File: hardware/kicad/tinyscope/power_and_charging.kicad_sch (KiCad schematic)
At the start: 44 parts

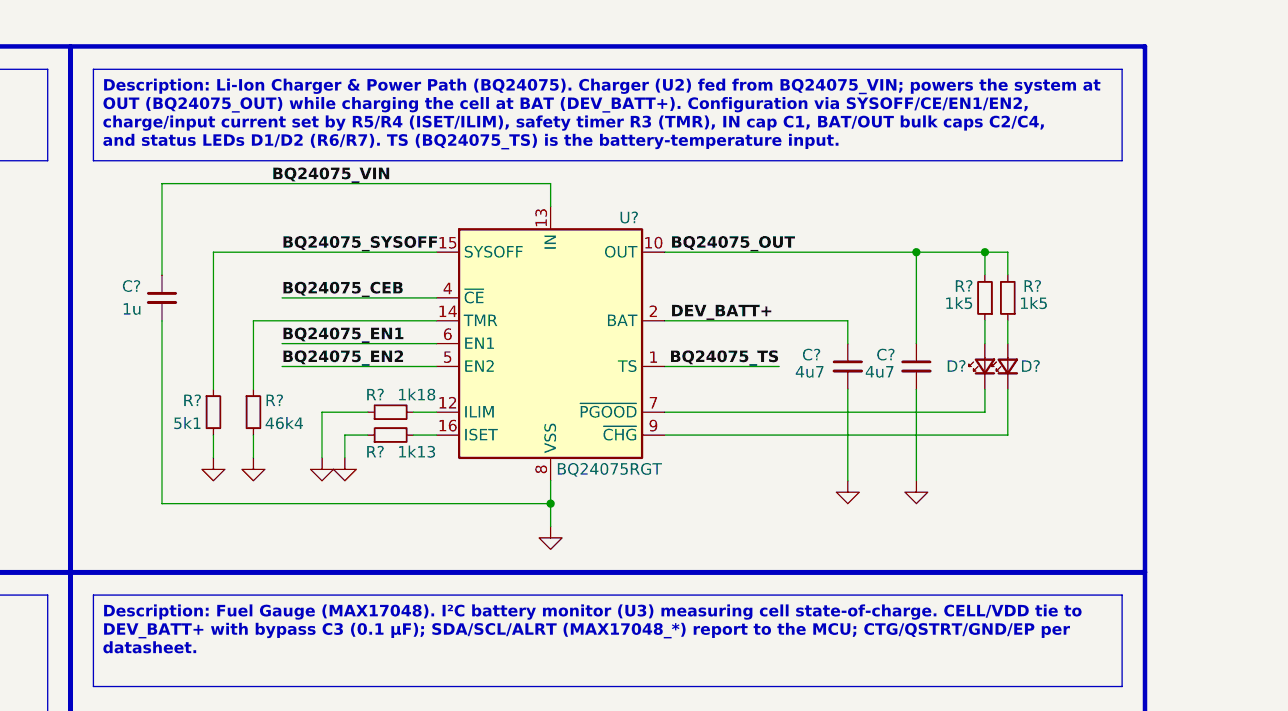
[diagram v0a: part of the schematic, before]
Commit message: feat: hardware: Adds on/off switch for BQ24075
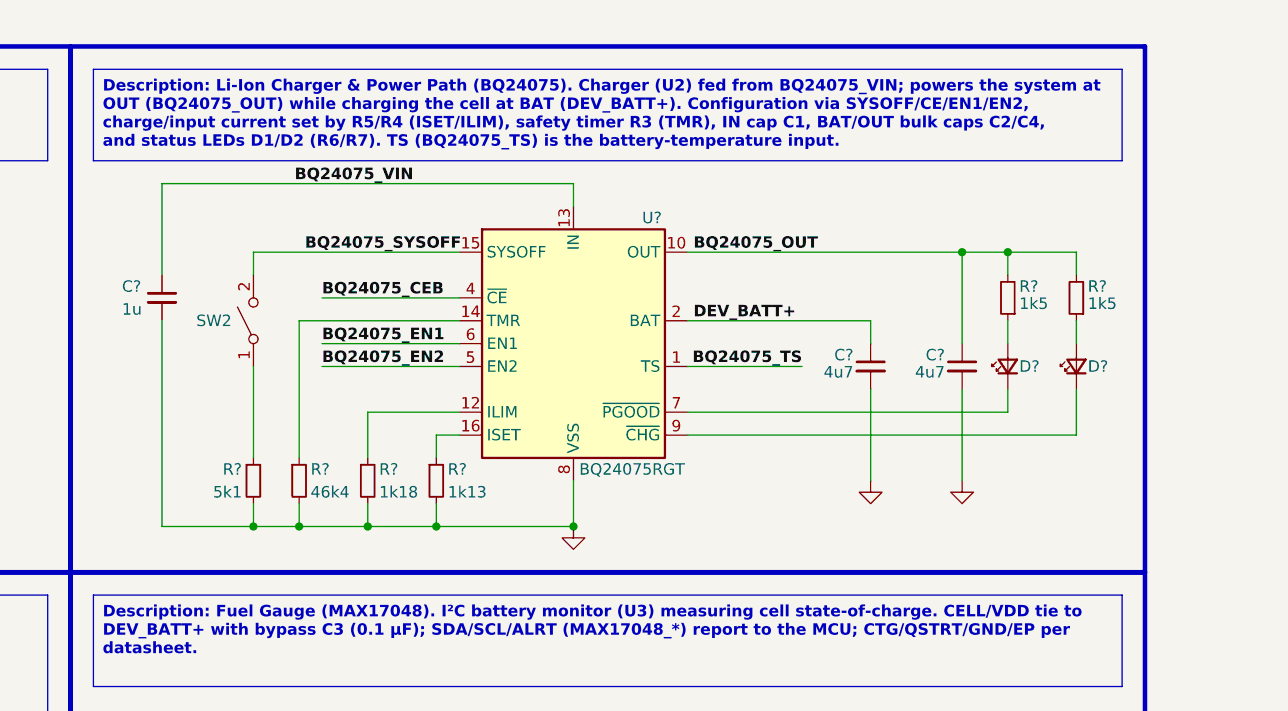
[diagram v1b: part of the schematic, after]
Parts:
- removed R?: 1k18, symbol Device:R_Small
- removed R?: 1k13, symbol Device:R_Small
- added R?: 1k13, symbol Device:R_Small
- added R?: 1k18, symbol Device:R_Small
- added SW2: SW_SPST, symbol Switch:SW_SPST
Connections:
- net BQ24075_SYSOFF: now also SW2.2 (B); no longer R?.1
- net GND: now also R?.2, R?.2
- net at U?.12 (ILIM): now also R?.1
- net at U?.16 (ISET): now also R?.1
- new net: R?.1, SW2.1 (A)
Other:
- moved on the sheet: C?, D?, R?, U?
